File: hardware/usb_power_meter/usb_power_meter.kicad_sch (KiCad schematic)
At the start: 7 parts, among them U1 nRF52833-QDxx, X1 32.768kHz crystal, X2 32Mhz crystal

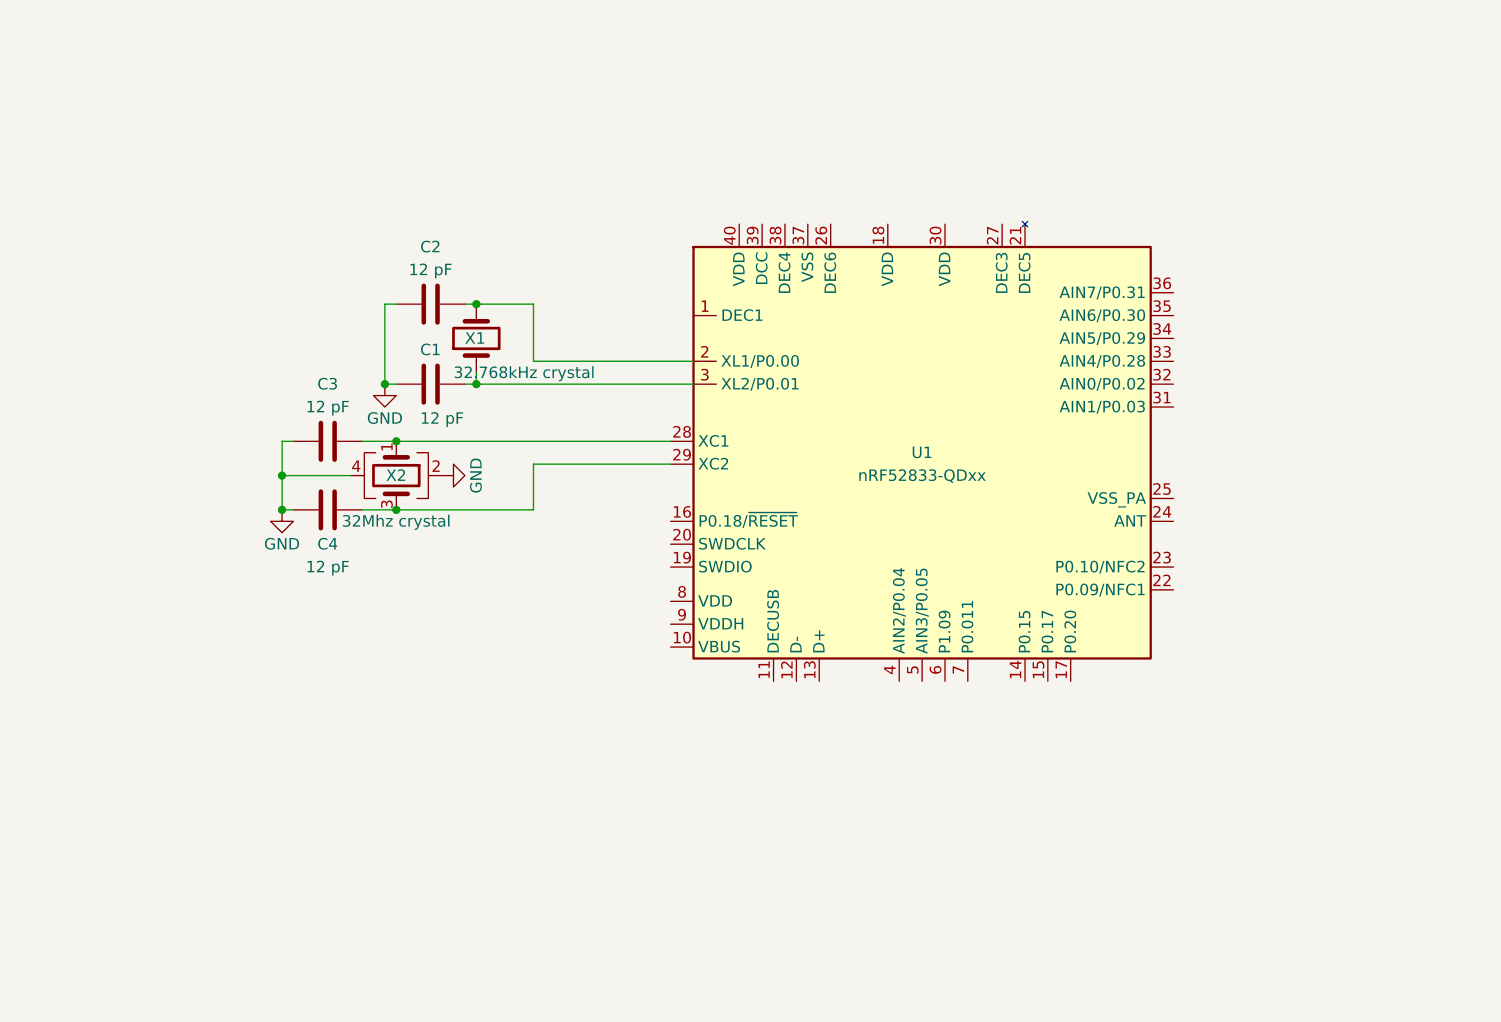
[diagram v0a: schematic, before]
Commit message: Add most of nRF52833 requirements (still need R1 and antenna stuff)
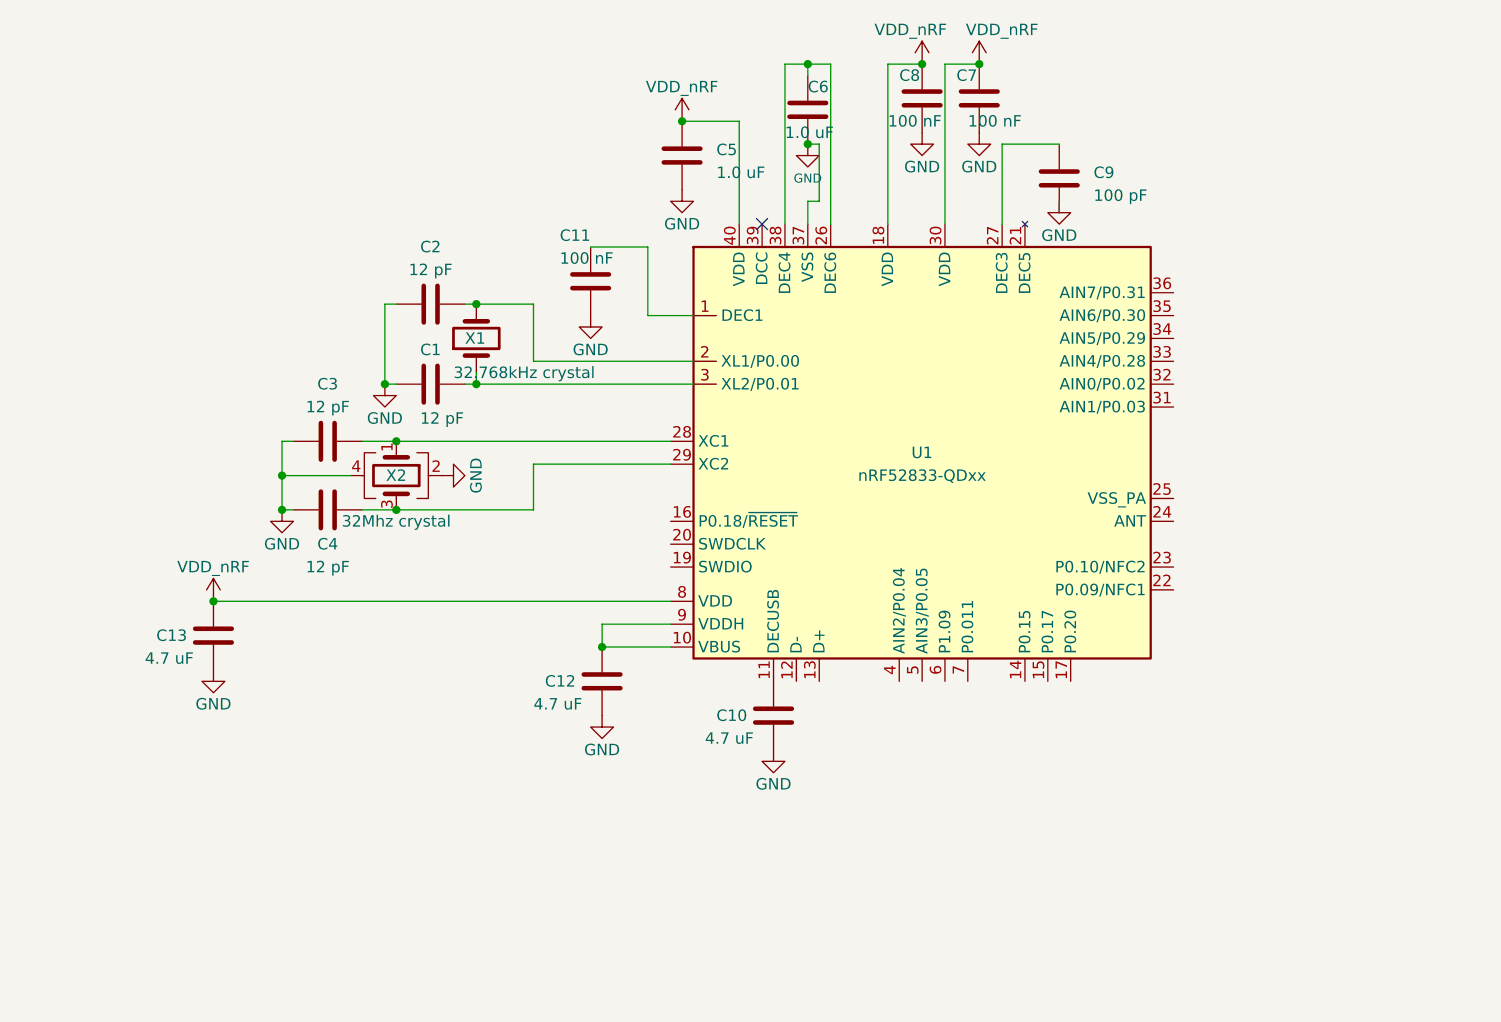
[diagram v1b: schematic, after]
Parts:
- added C10, C12, C13: 4.7 uF, Capacitor_SMD:C_0603_1608Metric, symbol Ostranna:4.7 uF
- added C11, C7, C8: 100 nF, Capacitor_SMD:C_0402_1005Metric, symbol Ostranna:100 nF
- added C5, C6: 1.0 uF, Capacitor_SMD:C_0603_1608Metric, symbol Ostranna:1.0 uF
- added C9: 100 pF, Capacitor_SMD:C_0402_1005Metric, symbol Ostranna:100 pF
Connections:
- net GND: now also U1.37 (VSS), C10.2, C11.1, C12.2, C13.2, C5.2, C6.2, C7.2, C8.2, C9.2
- net at U1.1 (DEC1): now also C11.2
- net at U1.10 (VBUS): now also U1.9 (VDDH), C12.1
- net at U1.11 (DECUSB): now also C10.1
- net VDD: now reaches U1.18 (VDD)
- net VDD: now also U1.30 (VDD), U1.40 (VDD), U1.8 (VDD), C13.1, C5.1, C7.1, C8.1
- net at U1.26 (DEC6): now also U1.38 (DEC4), C6.1
- net at U1.27 (DEC3): now also C9.1
- no-connect marks 0 -> 1

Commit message: Add series resistor
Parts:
- added R1: 2R2, Resistor_SMD:R_0402_1005Metric, symbol Ostranna:2R2
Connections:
- net at C12.1, U1.10 (VBUS), U1.9 (VDDH): now also R1.2
- new net VBUS: R1.1
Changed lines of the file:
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@@
+    (stroke (width 0) (type default))
+  )
+  (wire (pts (xy 99.06 127) (xy 110.49 127))
     (stroke (width 0) (type default))
   )
@@
         (path "/991df1c7-1ea4-4c32-892f-6236282859f6"
           (reference "C6") (unit 1)
+        )
+      )
+    )
+  )
+  (symbol (lib_id "power:VBUS") (at 91.44 127 0) (unit 1)
+    (in_bom yes) (on_board yes) (dnp no) (fields_autoplaced)
+    (property "Reference" "#PWR017" (at 91.44 130.81 0)
+      (effects (font (size 1.27 1.27)) hide)
+    )
+    (property "Value" "VBUS" (at 91.44 123.19 0)
+      (effects (font (size 1.27 1.27)))
+    )
+    (property "Footprint" "" (at 91.44 127 0)
+      (effects (font (size 1.27 1.27)) hide)
+    )
+    (property "Datasheet" "" (at 91.44 127 0)
+      (effects (font (size 1.27 1.27)) hide)
+    )
+    (pin "1")
+    (instances
+      (project "usb_power_meter"
+        (path "/991df1c7-1ea4-4c32-892f-6236282859f6"
+          (reference "#PWR017") (unit 1)
         )
       )
@@
         )
       )
+    )
+  )
+  (symbol (lib_id "Ostranna:2R2") (at 95.25 127 90) (unit 1)
+    (in_bom yes) (on_board yes) (dnp no)
+    (property "Reference" "R1" (at 95.25 124.46 90)
+      (effects (font (size 1.27 1.27)))
+    )
+    (property "Value" "2R2" (at 95.25 129.54 90)
+      (effects (font (size 1.27 1.27)))
+    )
+    (property "Footprint" "Resistor_SMD:R_0402_1005Metric" (at 95.25 128.778 90)
+      (effects (font (size 1.27 1.27)) hide)
+    )
+    (property "Datasheet" "~" (at 95.25 127 0)
+      (effects (font (size 1.27 1.27)) hide)
+    )
+    (property "LCSC" "C138013" (at 95.25 127 0)
+      (effects (font (size 1.27 1.27)) hide)
+    )
+    (pin "1")
+    (pin "2")
+    (instances
+      (project "usb_power_meter"
+        (path "/991df1c7-1ea4-4c32-892f-6236282859f6"
+          (reference "R1") (unit 1)
+        )
+      )

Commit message: Finish with nRF52833 required parts
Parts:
- added C14: 1.2 pF, Capacitor_SMD:C_0603_1608Metric, symbol Ostranna:1.2 pF
- added C15: 1.0 pF, Capacitor_SMD:C_0402_1005Metric, symbol Ostranna:1.0 pF
- added L1: 4.7 nH, Inductor_SMD:L_0402_1005Metric, symbol Ostranna:4.7 nH
- added L2: 2.2 nH, Inductor_SMD:L_0402_1005Metric, symbol Ostranna:2.2 nH
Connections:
- net GND: now also U1.25 (VSS_PA), C14.2, C15.2
- net at U1.24 (ANT): now also C15.1, L1.1
- new net: C14.1, L1.2, L2.1
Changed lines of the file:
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@@
   (junction (at 86.36 97.79) (diameter 0) (color 0 0 0 0)
   )
+  (junction (at 186.69 120.65) (diameter 0) (color 0 0 0 0)
+  )
   (junction (at 67.31 121.92) (diameter 0) (color 0 0 0 0)
   )
+  (junction (at 186.69 113.03) (diameter 0) (color 0 0 0 0)
+  )
   (junction (at 74.93 111.76) (diameter 0) (color 0 0 0 0)
   )
@@
   )
   (junction (at 152.4 62.23) (diameter 0) (color 0 0 0 0)
+  )
+  (junction (at 198.12 113.03) (diameter 0) (color 0 0 0 0)
   )
   (junction (at 87.63 104.14) (diameter 0) (color 0 0 0 0)
@@
     (stroke (width 0) (type default))
   )
+  (wire (pts (xy 187.96 113.03) (xy 186.69 113.03))
+    (stroke (width 0) (type default))
+  )
   (wire (pts (xy 102.87 95.25) (xy 102.87 88.9))
     (stroke (width 0) (type default))
@@
     (stroke (width 0) (type default))
   )
+  (wire (pts (xy 180.34 120.65) (xy 186.69 120.65))
+    (stroke (width 0) (type default))
+  )
   (wire (pts (xy 83.82 111.76) (xy 87.63 111.76))
     (stroke (width 0) (type default))
@@
     (stroke (width 0) (type default))
   )
+  (wire (pts (xy 173.99 113.03) (xy 186.69 113.03))
+    (stroke (width 0) (type default))
+  )
   (wire (pts (xy 148.59 80.01) (xy 148.59 62.23))
     (stroke (width 0) (type default))
   )
+  (wire (pts (xy 173.99 110.49) (xy 180.34 110.49))
+    (stroke (width 0) (type default))
+  )
   (wire (pts (xy 161.29 78.74) (xy 161.29 77.47))
     (stroke (width 0) (type default))
@@
     (stroke (width 0) (type default))
   )
+  (wire (pts (xy 180.34 110.49) (xy 180.34 120.65))
+    (stroke (width 0) (type default))
+  )
   (wire (pts (xy 154.94 80.01) (xy 154.94 71.12))
     (stroke (width 0) (type default))
@@
   )
   (wire (pts (xy 67.31 121.92) (xy 118.11 121.92))
+    (stroke (width 0) (type default))
+  )
+  (wire (pts (xy 195.58 113.03) (xy 198.12 113.03))
     (stroke (width 0) (type default))
   )
@@
     )
   )
+  (symbol (lib_id "Ostranna:2.2 nH") (at 201.93 113.03 90) (unit 1)
+    (in_bom yes) (on_board yes) (dnp no) (fields_autoplaced)
+    (property "Reference" "L2" (at 201.93 109.22 90)
+      (effects (font (size 1.27 1.27)))
+    )
+    (property "Value" "2.2 nH" (at 201.93 111.76 90)
+      (effects (font (size 1.27 1.27)))
+    )
+    (property "Footprint" "Inductor_SMD:L_0402_1005Metric" (at 201.93 113.03 0)
+      (effects (font (size 1.27 1.27)) hide)
+    )
+    (property "Datasheet" "~" (at 201.93 113.03 0)
+      (effects (font (size 1.27 1.27)) hide)
+    )
+    (property "LCSC" "C2044084" (at 201.93 113.03 0)
+      (effects (font (size 1.27 1.27)) hide)
+    )
+    (pin "1")
+    (pin "2")
+    (instances
+      (project "usb_power_meter"
+        (path "/991df1c7-1ea4-4c32-892f-6236282859f6"
+          (reference "L2") (unit 1)
+        )
+      )
+    )
+  )
   (symbol (lib_id "power:VDD") (at 67.31 121.92 0) (unit 1)
     (in_bom yes) (on_board yes) (dnp no) (fields_autoplaced)
@@
         (path "/991df1c7-1ea4-4c32-892f-6236282859f6"
           (reference "C1") (unit 1)
+        )
+      )
+    )
+  )
+  (symbol (lib_id "Ostranna:1.2 pF") (at 198.12 116.84 0) (unit 1)
+    (in_bom yes) (on_board yes) (dnp no)
+    (property "Reference" "C14" (at 200.66 115.57 0)
+      (effects (font (size 1.27 1.27)) (justify left))
+    )
+    (property "Value" "1.2 pF" (at 200.66 118.11 0)
+      (effects (font (size 1.27 1.27)) (justify left))
+    )
+    (property "Footprint" "Capacitor_SMD:C_0603_1608Metric" (at 199.0852 120.65 0)
+      (effects (font (size 1.27 1.27)) hide)
+    )
+    (property "Datasheet" "~" (at 198.12 116.84 0)
+      (effects (font (size 1.27 1.27)) hide)
+    )
+    (property "LCSC" "C913539" (at 198.12 116.84 0)
+      (effects (font (size 1.27 1.27)) hide)
+    )
+    (pin "1")
+    (pin "2")
+    (instances
+      (project "usb_power_meter"
+        (path "/991df1c7-1ea4-4c32-892f-6236282859f6"
+          (reference "C14") (unit 1)
         )
       )
@@
     )
   )
+  (symbol (lib_id "Ostranna:4.7 nH") (at 191.77 113.03 90) (unit 1)
+    (in_bom yes) (on_board yes) (dnp no) (fields_autoplaced)
+    (property "Reference" "L1" (at 191.77 109.22 90)
+      (effects (font (size 1.27 1.27)))
+    )
+    (property "Value" "4.7 nH" (at 191.77 111.76 90)
+      (effects (font (size 1.27 1.27)))
+    )
+    (property "Footprint" "Inductor_SMD:L_0402_1005Metric" (at 191.77 113.03 0)
+      (effects (font (size 1.27 1.27)) hide)
+    )
+    (property "Datasheet" "~" (at 191.77 113.03 0)
+      (effects (font (size 1.27 1.27)) hide)
+    )
+    (property "LCSC" "C2041409" (at 191.77 113.03 0)
+      (effects (font (size 1.27 1.27)) hide)
+    )
+    (pin "1")
+    (pin "2")
+    (instances
+      (project "usb_power_meter"
+        (path "/991df1c7-1ea4-4c32-892f-6236282859f6"
+          (reference "L1") (unit 1)
+        )
+      )
+    )
+  )
   (symbol (lib_id "Ostranna:100 nF") (at 109.22 86.36 180) (unit 1)
     (in_bom yes) (on_board yes) (dnp no)
@@
         (path "/991df1c7-1ea4-4c32-892f-6236282859f6"
           (reference "C11") (unit 1)
+        )
+      )
+    )
+  )
+  (symbol (lib_id "power:GND") (at 186.69 120.65 0) (unit 1)
+    (in_bom yes) (on_board yes) (dnp no)
+    (property "Reference" "#PWR018" (at 186.69 127 0)
+      (effects (font (size 1.27 1.27)) hide)
+    )
+    (property "Value" "GND" (at 186.69 124.46 0)
+      (effects (font (size 1.27 1.27)))
+    )
+    (property "Footprint" "" (at 186.69 120.65 0)
+      (effects (font (size 1.27 1.27)) hide)
+    )
+    (property "Datasheet" "" (at 186.69 120.65 0)
+      (effects (font (size 1.27 1.27)) hide)
+    )
+    (pin "1")
+    (instances
+      (project "usb_power_meter"
+        (path "/991df1c7-1ea4-4c32-892f-6236282859f6"
+          (reference "#PWR018") (unit 1)
         )
       )
@@
     )
   )
+  (symbol (lib_id "Ostranna:1.0 pF") (at 186.69 116.84 0) (unit 1)
+    (in_bom yes) (on_board yes) (dnp no)
+    (property "Reference" "C15" (at 189.23 115.57 0)
+      (effects (font (size 1.27 1.27)) (justify left))
+    )
+    (property "Value" "1.0 pF" (at 189.23 118.11 0)
+      (effects (font (size 1.27 1.27)) (justify left))
+    )
+    (property "Footprint" "Capacitor_SMD:C_0402_1005Metric" (at 187.6552 120.65 0)
+      (effects (font (size 1.27 1.27)) hide)
+    )
+    (property "Datasheet" "~" (at 186.69 116.84 0)
+      (effects (font (size 1.27 1.27)) hide)
+    )
+    (property "LCSC" "C72134" (at 186.69 116.84 0)
+      (effects (font (size 1.27 1.27)) hide)
+    )
+    (pin "1")
+    (pin "2")
+    (instances
+      (project "usb_power_meter"
+        (path "/991df1c7-1ea4-4c32-892f-6236282859f6"
+          (reference "C15") (unit 1)
+        )
+      )
+    )
+  )
   (symbol (lib_id "Ostranna:32Mhz crystal") (at 87.63 107.95 270) (unit 1)
     (in_bom yes) (on_board yes) (dnp no)
@@
         )
       )
+    )
+  )
+  (symbol (lib_id "power:GND") (at 198.12 120.65 0) (unit 1)
+    (in_bom yes) (on_board yes) (dnp no)
+    (property "Reference" "#PWR019" (at 198.12 127 0)
+      (effects (font (size 1.27 1.27)) hide)
+    )
+    (property "Value" "GND" (at 198.12 124.46 0)
+      (effects (font (size 1.27 1.27)))
+    )
+    (property "Footprint" "" (at 198.12 120.65 0)
+      (effects (font (size 1.27 1.27)) hide)
+    )
+    (property "Datasheet" "" (at 198.12 120.65 0)
+      (effects (font (size 1.27 1.27)) hide)
+    )
+    (pin "1")
+    (instances
+      (project "usb_power_meter"
+        (path "/991df1c7-1ea4-4c32-892f-6236282859f6"
+          (reference "#PWR019") (unit 1)
+        )
+      )
